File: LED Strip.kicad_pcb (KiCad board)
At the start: 2 copper layers, 21 x 12 mm, 9 parts, among them J1 CONN_01X02

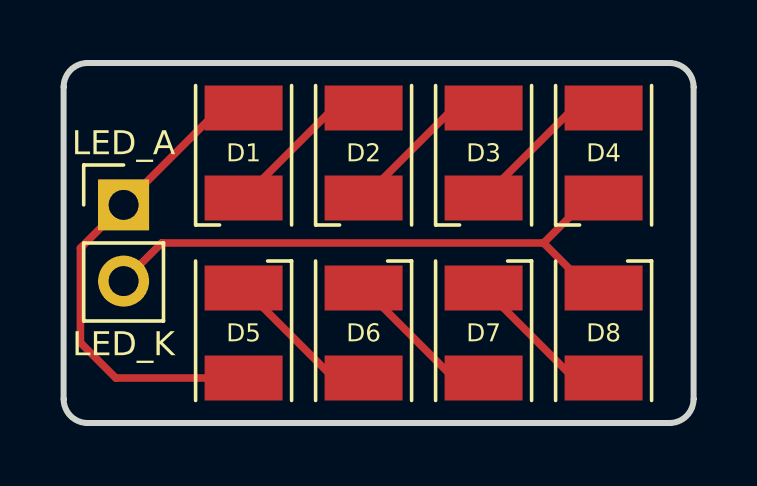
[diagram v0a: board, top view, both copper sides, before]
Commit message: Reduced size of board to 12 x 20 mm, redid some tracks
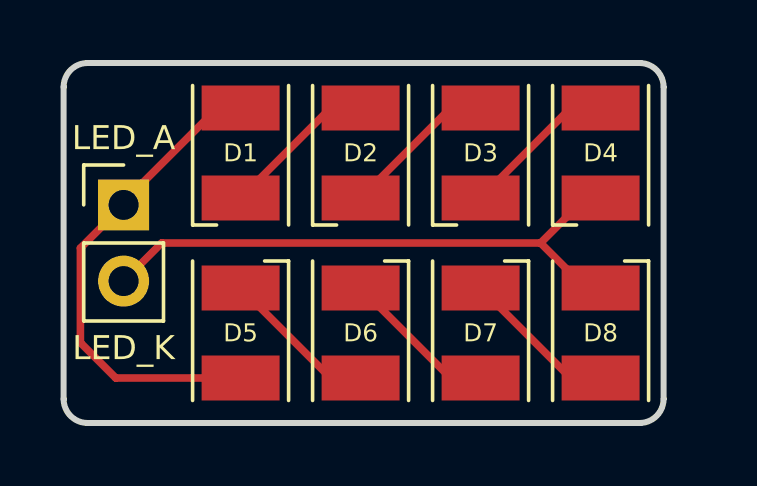
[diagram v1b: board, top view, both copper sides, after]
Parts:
- moved D1 0.10 mm to (105.9, 91.0)
- moved D2 0.10 mm to (109.9, 91.0)
- moved D3 0.10 mm to (113.9, 91.0)
- moved D4 0.10 mm to (117.9, 91.0)
- moved D5 0.10 mm to (105.9, 97.0)
- moved D6 0.10 mm to (109.9, 97.0)
- moved D7 0.10 mm to (113.9, 97.0)
- moved D8 0.10 mm to (117.9, 97.0)
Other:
- board size 21 x 12 mm -> 20 x 12 mm
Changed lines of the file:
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@@
     (links 10)
     (no_connects 0)
-    (area 99.899999 87.899999 121.100001 100.100001)
+    (area 99.899999 87.899999 120.100001 100.100001)
     (thickness 1.6)
     (drawings 10)
@@
     (pad_to_mask_clearance 0.2)
     (aux_axis_origin 0 0)
+    (grid_origin 99.99 99.99)
     (visible_elements 7FFEFF7F)
     (pcbplotparams
@@
   )
   (module LEDs:LED_PLCC-2 (layer Top)
-    (at 106 91 90)
+    (at 105.9 91 90)
     (descr "LED PLCC-2 SMD package")
     (tags "LED PLCC-2 SMD")
@@
   )
   (module LEDs:LED_PLCC-2 (layer Top)
-    (at 110 91 90)
+    (at 109.9 91 90)
     (descr "LED PLCC-2 SMD package")
     (tags "LED PLCC-2 SMD")
@@
   )
   (module LEDs:LED_PLCC-2 (layer Top)
-    (at 114 91 90)
+    (at 113.9 91 90)
     (descr "LED PLCC-2 SMD package")
     (tags "LED PLCC-2 SMD")
@@
   )
   (module LEDs:LED_PLCC-2 (layer Top)
-    (at 118 91 90)
+    (at 117.9 91 90)
     (descr "LED PLCC-2 SMD package")
     (tags "LED PLCC-2 SMD")
@@
   )
   (module LEDs:LED_PLCC-2 (layer Top)
-    (at 106 97 270)
+    (at 105.9 97 270)
     (descr "LED PLCC-2 SMD package")
     (tags "LED PLCC-2 SMD")
@@
   )
   (module LEDs:LED_PLCC-2 (layer Top)
-    (at 110 97 270)
+    (at 109.9 97 270)
     (descr "LED PLCC-2 SMD package")
     (tags "LED PLCC-2 SMD")
@@
   )
   (module LEDs:LED_PLCC-2 (layer Top)
-    (at 114 97 270)
+    (at 113.9 97 270)
     (descr "LED PLCC-2 SMD package")
     (tags "LED PLCC-2 SMD")
@@
   )
   (module LEDs:LED_PLCC-2 (layer Top)
-    (at 118 97 270)
+    (at 117.9 97 270)
     (descr "LED PLCC-2 SMD package")
     (tags "LED PLCC-2 SMD")
@@
     )
   )
-  (gr_text LED_K (at 102 97.37) (layer F.SilkS)
+  (gr_text LED_K (at 102 97.5) (layer F.SilkS)
     (effects (font (size 0.8 0.8) (thickness 0.18)))
   )
-  (gr_text LED_A (at 102 90.67) (layer F.SilkS)
+  (gr_text LED_A (at 102 90.5) (layer F.SilkS)
     (effects (font (size 0.8 0.8) (thickness 0.18)))
   )
-  (gr_arc (start 120.2 99.2) (end 121 99.2) (angle 90) (layer Edge.Cuts) (width 0.2))
-  (gr_arc (start 120.2 88.8) (end 120.2 88) (angle 90) (layer Edge.Cuts) (width 0.2))
+  (gr_arc (start 119.2 99.2) (end 120 99.2) (angle 90) (layer Edge.Cuts) (width 0.2))
+  (gr_arc (start 119.2 88.8) (end 119.2 88) (angle 90) (layer Edge.Cuts) (width 0.2))
   (gr_arc (start 100.8 88.8) (end 100 88.8) (angle 90) (layer Edge.Cuts) (width 0.2))
   (gr_arc (start 100.8 99.2) (end 100.8 100) (angle 90) (layer Edge.Cuts) (width 0.2))
   (gr_line (start 100 99.2) (end 100 88.8) (angle 90) (layer Edge.Cuts) (width 0.2))
-  (gr_line (start 121 99.2) (end 121 88.8) (angle 90) (layer Edge.Cuts) (width 0.2))
-  (gr_line (start 100.8 88) (end 120.2 88) (angle 90) (layer Edge.Cuts) (width 0.2))
-  (gr_line (start 100.8 100) (end 120.2 100) (angle 90) (layer Edge.Cuts) (width 0.2))
-  (segment (start 106 92.5) (end 109 89.5) (width 0.254) (layer Top) (net 1))
-  (segment (start 109 89.5) (end 110 89.5) (width 0.254) (layer Top) (net 1))
-  (segment (start 102 92.73) (end 100.56 94.17) (width 0.254) (layer Top) (net 2))
-  (segment (start 101.74 98.5) (end 106 98.5) (width 0.254) (layer Top) (net 2))
+  (gr_line (start 120 99.2) (end 120 88.8) (angle 90) (layer Edge.Cuts) (width 0.2))
+  (gr_line (start 100.8 88) (end 119.2 88) (angle 90) (layer Edge.Cuts) (width 0.2))
+  (gr_line (start 100.8 100) (end 119.2 100) (angle 90) (layer Edge.Cuts) (width 0.2))
+  (segment (start 105.9 92.5) (end 108.9 89.5) (width 0.254) (layer Top) (net 1) (status C00000))
+  (segment (start 108.9 89.5) (end 109.9 89.5) (width 0.254) (layer Top) (net 1) (status C00000))
+  (segment (start 105.9 98.5) (end 101.74 98.5) (width 0.254) (layer Top) (net 2) (status 400000))
+  (segment (start 100.56 94.17) (end 100.56 97.32) (width 0.254) (layer Top) (net 2))
   (segment (start 100.56 97.32) (end 101.74 98.5) (width 0.254) (layer Top) (net 2))
-  (segment (start 100.56 94.17) (end 100.56 97.32) (width 0.254) (layer Top) (net 2))
-  (segment (start 102 92.73) (end 105.23 89.5) (width 0.254) (layer Top) (net 2))
-  (segment (start 105.23 89.5) (end 106 89.5) (width 0.254) (layer Top) (net 2))
-  (segment (start 110 92.5) (end 113 89.5) (width 0.254) (layer Top) (net 3))
-  (segment (start 113 89.5) (end 114 89.5) (width 0.254) (layer Top) (net 3))
-  (segment (start 114 92.5) (end 117 89.5) (width 0.254) (layer Top) (net 4))
-  (segment (start 117 89.5) (end 118 89.5) (width 0.254) (layer Top) (net 4))
-  (segment (start 106 95.5) (end 109 98.5) (width 0.254) (layer Top) (net 5))
-  (segment (start 109 98.5) (end 110 98.5) (width 0.254) (layer Top) (net 5))
-  (segment (start 110 95.5) (end 113 98.5) (width 0.254) (layer Top) (net 6))
-  (segment (start 113 98.5) (end 114 98.5) (width 0.254) (layer Top) (net 6))
-  (segment (start 116 94) (end 103.27 94) (width 0.254) (layer Top) (net 7))
-  (segment (start 103.27 94) (end 102 95.27) (width 0.254) (layer Top) (net 7))
-  (segment (start 117.5 95.5) (end 116 94) (width 0.254) (layer Top) (net 7))
-  (segment (start 116 94) (end 117.5 92.5) (width 0.254) (layer Top) (net 7))
-  (segment (start 117.5 95.5) (end 118 95.5) (width 0.254) (layer Top) (net 7))
-  (segment (start 118 92.5) (end 117.5 92.5) (width 0.254) (layer Top) (net 7))
-  (segment (start 114 95.5) (end 117 98.5) (width 0.254) (layer Top) (net 8))
-  (segment (start 117 98.5) (end 118 98.5) (width 0.254) (layer Top) (net 8))
+  (segment (start 100.56 94.17) (end 102 92.73) (width 0.254) (layer Top) (net 2))
+  (segment (start 101.9 92.73) (end 105.13 89.5) (width 0.254) (layer Top) (net 2))
+  (segment (start 105.13 89.5) (end 105.9 89.5) (width 0.254) (layer Top) (net 2))
+  (segment (start 109.9 92.5) (end 112.9 89.5) (width 0.254) (layer Top) (net 3) (status C00000))
+  (segment (start 112.9 89.5) (end 113.9 89.5) (width 0.254) (layer Top) (net 3) (status C00000))
+  (segment (start 113.9 92.5) (end 116.9 89.5) (width 0.254) (layer Top) (net 4) (status C00000))
+  (segment (start 116.9 89.5) (end 117.9 89.5) (width 0.254) (layer Top) (net 4) (status C00000))
+  (segment (start 105.9 95.5) (end 108.9 98.5) (width 0.254) (layer Top) (net 5) (status C00000))
+  (segment (start 108.9 98.5) (end 109.9 98.5) (width 0.254) (layer Top) (net 5) (status C00000))
+  (segment (start 109.9 95.5) (end 112.9 98.5) (width 0.254) (layer Top) (net 6) (status C00000))
+  (segment (start 112.9 98.5) (end 113.9 98.5) (width 0.254) (layer Top) (net 6) (status C00000))
+  (segment (start 115.9 94) (end 103.27 94) (width 0.254) (layer Top) (net 7))
+  (segment (start 103.27 94) (end 102 95.27) (width 0.254) (layer Top) (net 7) (status 800000))
+  (segment (start 117.4 95.5) (end 115.9 94) (width 0.254) (layer Top) (net 7))
+  (segment (start 115.9 94) (end 117.4 92.5) (width 0.254) (layer Top) (net 7))
+  (segment (start 117.4 95.5) (end 117.9 95.5) (width 0.254) (layer Top) (net 7))
+  (segment (start 117.9 92.5) (end 117.4 92.5) (width 0.254) (layer Top) (net 7))
+  (segment (start 113.9 95.5) (end 116.9 98.5) (width 0.254) (layer Top) (net 8) (status C00000))
+  (segment (start 116.9 98.5) (end 117.9 98.5) (width 0.254) (layer Top) (net 8) (status C00000))
 )

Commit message: Adds copper pours to top and bottom layers
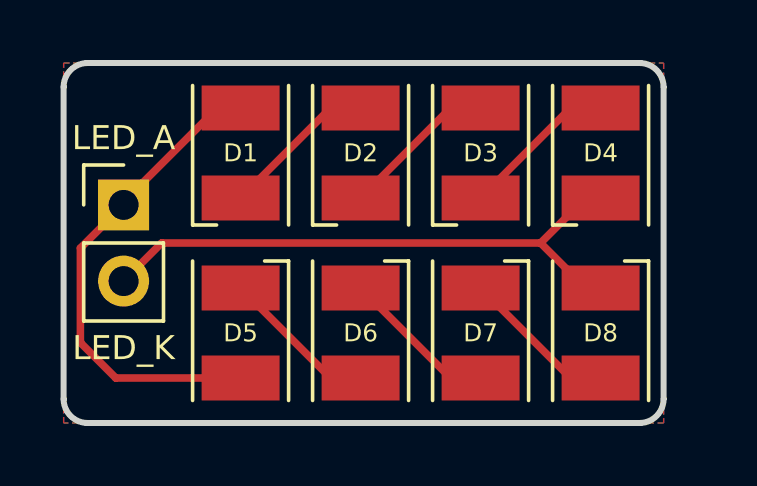
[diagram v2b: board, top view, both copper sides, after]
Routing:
- added copper zone on B.Cu, net (none)
- added copper zone on F.Cu, net (none)
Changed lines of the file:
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@@
     (last_trace_width 0.254)
     (trace_clearance 0.254)
-    (zone_clearance 0.508)
+    (zone_clearance 0.254)
     (zone_45_only no)
     (trace_min 0.2)
@@
     (pad_to_mask_clearance 0.2)
     (aux_axis_origin 0 0)
-    (grid_origin 99.99 99.99)
+    (grid_origin 100 100)
     (visible_elements 7FFEFF7F)
     (pcbplotparams
@@
   (gr_line (start 100.8 88) (end 119.2 88) (angle 90) (layer Edge.Cuts) (width 0.2))
   (gr_line (start 100.8 100) (end 119.2 100) (angle 90) (layer Edge.Cuts) (width 0.2))
-  (segment (start 105.9 92.5) (end 108.9 89.5) (width 0.254) (layer Top) (net 1) (status C00000))
-  (segment (start 108.9 89.5) (end 109.9 89.5) (width 0.254) (layer Top) (net 1) (status C00000))
-  (segment (start 105.9 98.5) (end 101.74 98.5) (width 0.254) (layer Top) (net 2) (status 400000))
+  (segment (start 105.9 92.5) (end 108.9 89.5) (width 0.254) (layer Top) (net 1))
+  (segment (start 108.9 89.5) (end 109.9 89.5) (width 0.254) (layer Top) (net 1))
+  (segment (start 105.9 98.5) (end 101.74 98.5) (width 0.254) (layer Top) (net 2))
   (segment (start 100.56 94.17) (end 100.56 97.32) (width 0.254) (layer Top) (net 2))
   (segment (start 100.56 97.32) (end 101.74 98.5) (width 0.254) (layer Top) (net 2))
@@
   (segment (start 101.9 92.73) (end 105.13 89.5) (width 0.254) (layer Top) (net 2))
   (segment (start 105.13 89.5) (end 105.9 89.5) (width 0.254) (layer Top) (net 2))
-  (segment (start 109.9 92.5) (end 112.9 89.5) (width 0.254) (layer Top) (net 3) (status C00000))
-  (segment (start 112.9 89.5) (end 113.9 89.5) (width 0.254) (layer Top) (net 3) (status C00000))
-  (segment (start 113.9 92.5) (end 116.9 89.5) (width 0.254) (layer Top) (net 4) (status C00000))
-  (segment (start 116.9 89.5) (end 117.9 89.5) (width 0.254) (layer Top) (net 4) (status C00000))
-  (segment (start 105.9 95.5) (end 108.9 98.5) (width 0.254) (layer Top) (net 5) (status C00000))
-  (segment (start 108.9 98.5) (end 109.9 98.5) (width 0.254) (layer Top) (net 5) (status C00000))
-  (segment (start 109.9 95.5) (end 112.9 98.5) (width 0.254) (layer Top) (net 6) (status C00000))
-  (segment (start 112.9 98.5) (end 113.9 98.5) (width 0.254) (layer Top) (net 6) (status C00000))
+  (segment (start 109.9 92.5) (end 112.9 89.5) (width 0.254) (layer Top) (net 3))
+  (segment (start 112.9 89.5) (end 113.9 89.5) (width 0.254) (layer Top) (net 3))
+  (segment (start 113.9 92.5) (end 116.9 89.5) (width 0.254) (layer Top) (net 4))
+  (segment (start 116.9 89.5) (end 117.9 89.5) (width 0.254) (layer Top) (net 4))
+  (segment (start 105.9 95.5) (end 108.9 98.5) (width 0.254) (layer Top) (net 5))
+  (segment (start 108.9 98.5) (end 109.9 98.5) (width 0.254) (layer Top) (net 5))
+  (segment (start 109.9 95.5) (end 112.9 98.5) (width 0.254) (layer Top) (net 6))
+  (segment (start 112.9 98.5) (end 113.9 98.5) (width 0.254) (layer Top) (net 6))
   (segment (start 115.9 94) (end 103.27 94) (width 0.254) (layer Top) (net 7))
-  (segment (start 103.27 94) (end 102 95.27) (width 0.254) (layer Top) (net 7) (status 800000))
+  (segment (start 103.27 94) (end 102 95.27) (width 0.254) (layer Top) (net 7))
   (segment (start 117.4 95.5) (end 115.9 94) (width 0.254) (layer Top) (net 7))
   (segment (start 115.9 94) (end 117.4 92.5) (width 0.254) (layer Top) (net 7))
   (segment (start 117.4 95.5) (end 117.9 95.5) (width 0.254) (layer Top) (net 7))
   (segment (start 117.9 92.5) (end 117.4 92.5) (width 0.254) (layer Top) (net 7))
-  (segment (start 113.9 95.5) (end 116.9 98.5) (width 0.254) (layer Top) (net 8) (status C00000))
-  (segment (start 116.9 98.5) (end 117.9 98.5) (width 0.254) (layer Top) (net 8) (status C00000))
+  (segment (start 113.9 95.5) (end 116.9 98.5) (width 0.254) (layer Top) (net 8))
+  (segment (start 116.9 98.5) (end 117.9 98.5) (width 0.254) (layer Top) (net 8))
+  (zone (net 0) (net_name "") (layer Top) (hatch edge 0.508)
+    (connect_pads (clearance 0.254))
+    (min_thickness 0.254)
+    (fill yes (arc_segments 16) (thermal_gap 0.508) (thermal_bridge_width 1.27))
+    (polygon
+      (pts
+        (xy 120 100) (xy 100 100) (xy 100 88) (xy 120 88)
+      )
+    )
+  )
+  (zone (net 0) (net_name "") (layer Bottom) (hatch edge 0.508)
+    (connect_pads (clearance 0.254))
+    (min_thickness 0.254)
+    (fill yes (arc_segments 16) (thermal_gap 0.508) (thermal_bridge_width 1.27))
+    (polygon
+      (pts
+        (xy 120 100) (xy 100 100) (xy 100 88) (xy 120 88)
+      )
+    )
+  )
 )
